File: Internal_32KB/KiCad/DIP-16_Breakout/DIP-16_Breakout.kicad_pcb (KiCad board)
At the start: 2 copper layers, 10.8 x 21.6 mm, 2 parts, among them J1 DIP-16 Socket, J2 Breakout

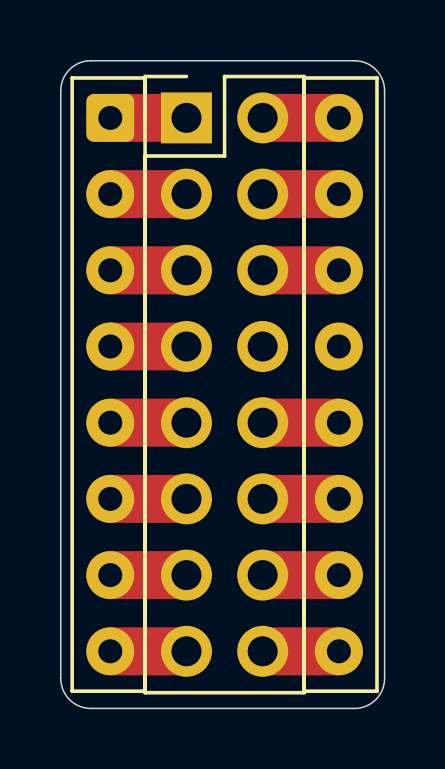
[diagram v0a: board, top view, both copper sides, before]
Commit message: Silkscreen improvements
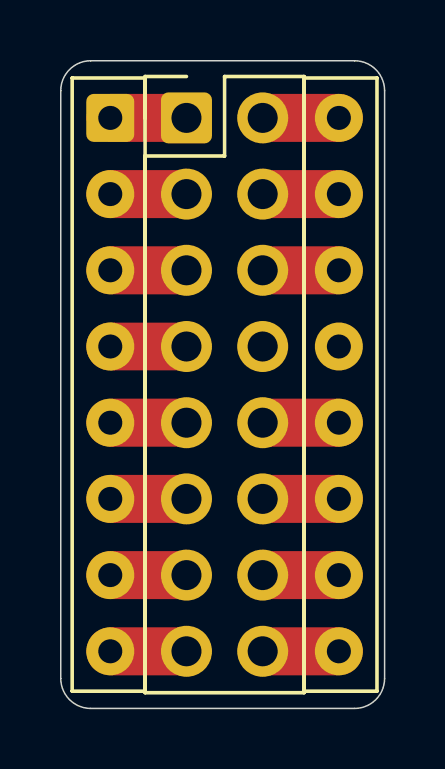
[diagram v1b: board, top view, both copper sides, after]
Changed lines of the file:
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@@
 			)
 		)
-		(pad "1" thru_hole rect
+		(pad "1" thru_hole roundrect
 			(at 0 0)
 			(size 1.7 1.7)
@@
 			(layers "*.Cu" "*.Mask")
 			(remove_unused_layers no)
+			(roundrect_rratio 0.1470588235)
 			(net 5 "Net-(J1-Pin_1)")
 			(pinfunction "Pin_1")
